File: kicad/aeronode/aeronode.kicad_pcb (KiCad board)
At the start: 4 copper layers, 90 x 70 mm, 77 parts, among them J1 IMU_BOARD, J2 USB-C PD / recovery, J3 2S LiFePO4 6Ah + BMS, Q1 NMOS pass - TBD, SW1 ON/OFF, U1 ConnectCore93_LGA, U10 BMP390, U2 CYPD3177-24LQ, U3 BQ25798, U4 LMR33630ADDA, U5 LTC4364CMS, U6 BME690, U7 DAN-F10N, U9 MMC5983MA

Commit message: [LIMA] kicad: FIX - USB-C ground was never connected to system GND
J2's four GND pins (A1/A12/B1/B12) are stacked on one connection point in the
USB_C_Receptacle_USB2.0_16P symbol, so they formed their own 4-node net
'Net-(J2-GND-PadA1)' with no wire and no label attaching them to /GND. The
SHIELD pin was likewise floating. /GND had 254 nodes and J2 was not among them.

Impact if built: VBUS arrives with no return path. No charging, no PD
negotiation, CC1/CC2 with no ground reference - the board is dead on USB.

ERC did not surface it usefully: the pins are connected to EACH OTHER, so they
are not 'unconnected pins', and the design already carries 170 pin_not_connected
warnings from unused CC93 pads, which buries anything real. It was found by
inspecting net pad-counts while planning the ground plane.

Fix: added GND labels at (149.86,642.62) and (142.24,642.62) - this schematic
uses local labels, not power symbols, so that is the idiomatic form here.
/GND now 259 nodes with J2 A1/A12/B1/B12/SH present, no isolated J2 nets.
Board re-bound from the corrected netlist: 8 pads changed, 0 mismatches,
DRC 0 violations, schematic parity 0.

Shield is tied directly to GND. Standard for a board with no separate chassis
ground, but revisit if the enclosure needs a decoupled shield connection.

Co-Authored-By: Claude Opus 5 <noreply@anthropic.com>
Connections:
- J2 pad A1: Net-(J2-GND-PadA1) -> /GND
- J2 pad A12: Net-(J2-GND-PadA1) -> /GND
- J2 pad B1: Net-(J2-GND-PadA1) -> /GND
- J2 pad B12: Net-(J2-GND-PadA1) -> /GND
- J2 pad SH: unconnected-(J2-SHIELD-PadSH) -> /GND
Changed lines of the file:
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@@
 			(layers "F.Cu" "F.Mask" "F.Paste")
 			(roundrect_rratio 0.25)
-			(net "Net-(J2-GND-PadA1)")
+			(net "/GND")
 		)
 		(pad "A4" smd roundrect
@@
 			(layers "F.Cu" "F.Mask" "F.Paste")
 			(roundrect_rratio 0.25)
-			(net "Net-(J2-GND-PadA1)")
+			(net "/GND")
 		)
 		(pad "B1" smd roundrect
@@
 			(layers "F.Cu" "F.Mask" "F.Paste")
 			(roundrect_rratio 0.25)
-			(net "Net-(J2-GND-PadA1)")
+			(net "/GND")
 		)
 		(pad "B4" smd roundrect
@@
 			(layers "F.Cu" "F.Mask" "F.Paste")
 			(roundrect_rratio 0.25)
-			(net "Net-(J2-GND-PadA1)")
+			(net "/GND")
 		)
 		(pad "SH" thru_hole oval
@@
 			(layers "*.Cu" "*.Mask")
 			(remove_unused_layers no)
-			(net "unconnected-(J2-SHIELD-PadSH)")
+			(net "/GND")
 		)
 		(pad "SH" thru_hole oval
@@
 			(layers "*.Cu" "*.Mask")
 			(remove_unused_layers no)
-			(net "unconnected-(J2-SHIELD-PadSH)")
+			(net "/GND")
 		)
 		(pad "SH" thru_hole oval
@@
 			(layers "*.Cu" "*.Mask")
 			(remove_unused_layers no)
-			(net "unconnected-(J2-SHIELD-PadSH)")
+			(net "/GND")
 		)
 		(pad "SH" thru_hole oval
@@
 			(layers "*.Cu" "*.Mask")
 			(remove_unused_layers no)
-			(net "unconnected-(J2-SHIELD-PadSH)")
+			(net "/GND")
 		)
 		(embedded_fonts no)

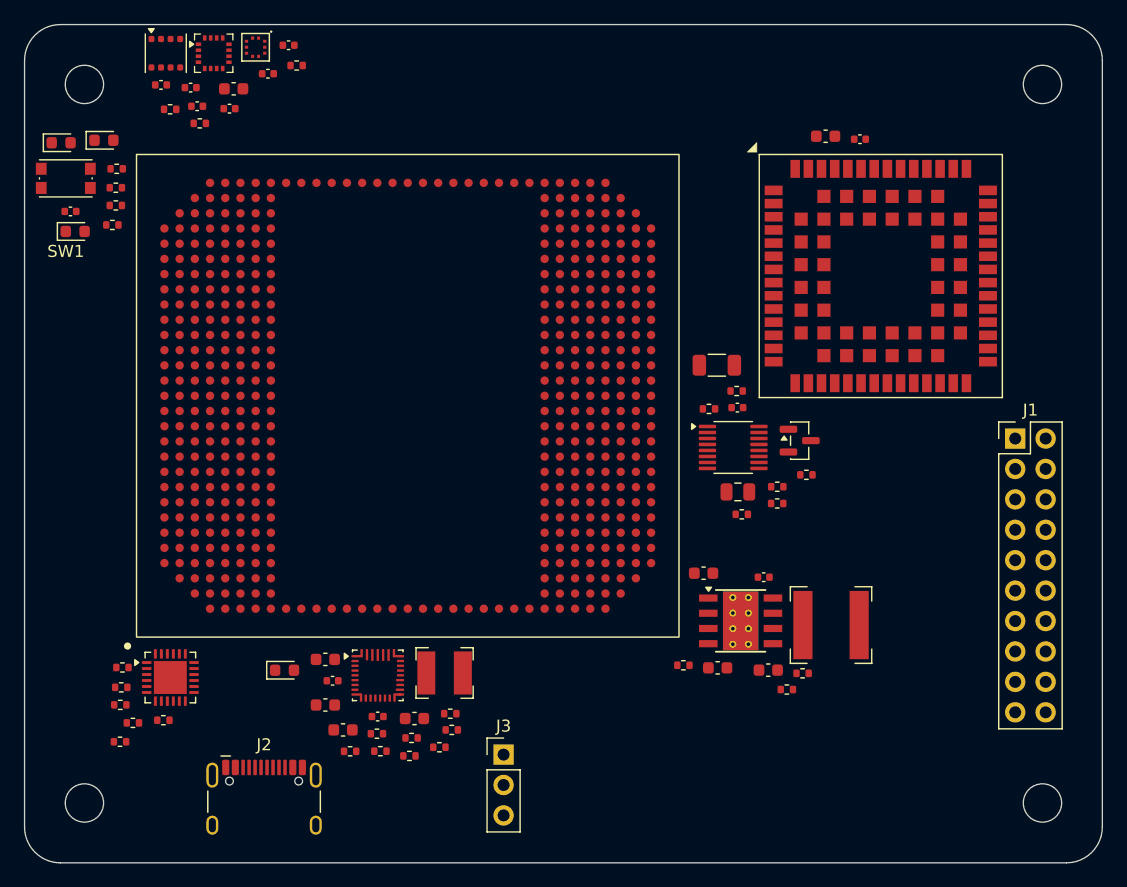
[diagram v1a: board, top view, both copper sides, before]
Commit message: [LIMA] kicad: add GND/+3V3 planes, net classes and via stitching
Stackup now SIG/GND/PWR/SIG: solid GND plane on In1 under F.Cu so top-layer
signals reference an unbroken return; +3V3 plane on In2 (the only rail spanning
the whole board, 37 pads across x 26.8..102.7). Localised rails stay as traces.

Net classes: Default 0.20mm, Power 0.50mm, HighCurrent 1.00mm. All at 0.20mm
clearance - HighCurrent started at 0.25mm and failed against fixed IC pin pitch
inside U3/U5; current is carried by width, not clearance.

266 GND stitching vias on a 4mm grid tie the pours to the In1 plane. 31 of 37
+3V3 pads have a fanout via to In2; 6 failed in the tight sensor cluster and
need hand routing or a smaller local via.

DRC 0 violations, parity 0, unconnected 468 -> 141.

Four bugs in my own via placement, all caught by DRC and all recorded:
- 0.25mm drills below the 0.30mm board minimum
- hole-to-hole check skipped same-net pads, but hole spacing is net-independent;
  GND vias landed 0.08mm from J1's GND through-holes
- track PATHS were never validated, only via positions, so tracks crossed pads
  and shorted +3V3 to BAT_TS and to U10's INT pin
- dangling vias where the pour did not reach
Lesson: validating an endpoint is not validating a connection.

Also recorded a KiCad SWIG trap: board.Remove() in a loop leaves GetTracks()/
GetFootprints() returning raw SwigPyObjects. Save and reload between bulk
deletion and rebuild.

Signal routing is NOT done - no autorouter is available.

Co-Authored-By: Claude Opus 5 <noreply@anthropic.com>
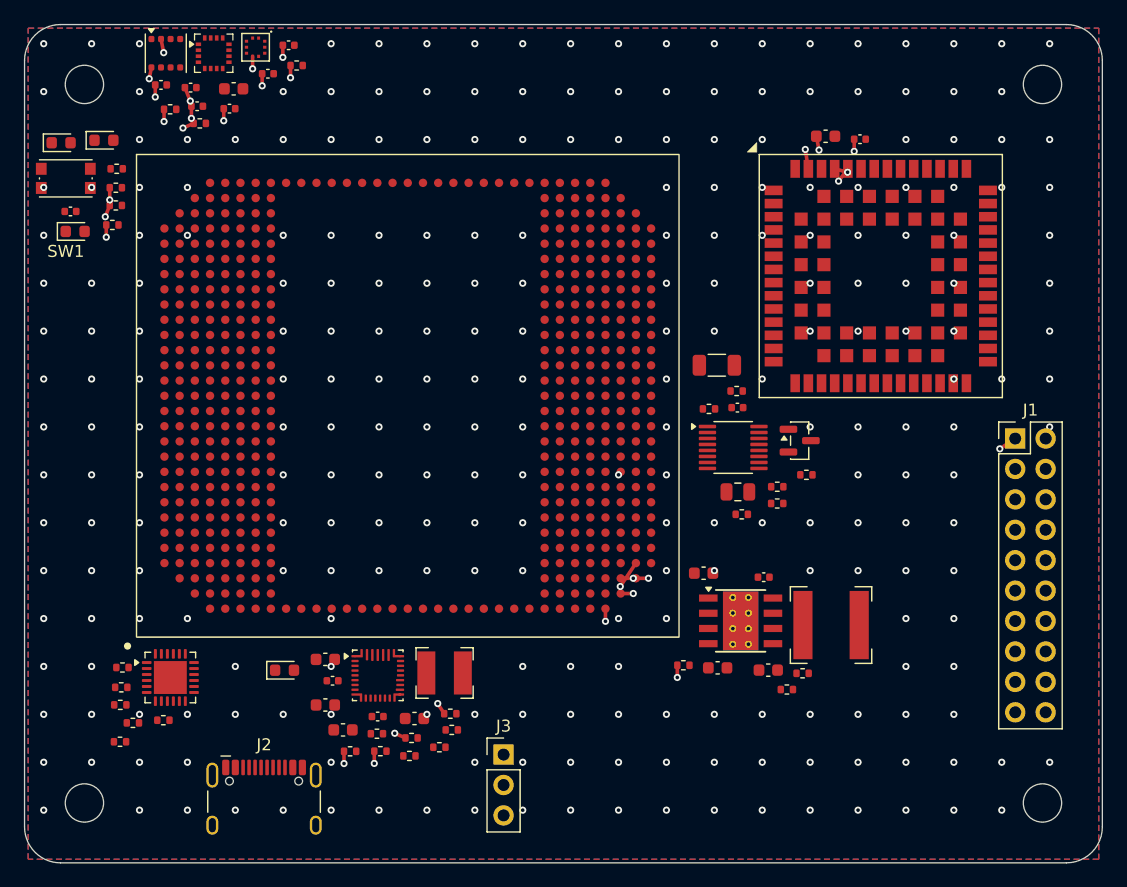
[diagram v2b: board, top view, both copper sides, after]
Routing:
- net /+3V3: track 0.00 -> 34.9 mm, vias 0 -> 31
- net /GND: vias 0 -> 266
- added copper zone on In2.Cu, net /+3V3
- added copper zone on B.Cu, net /GND
- added copper zone on F.Cu, net /GND
- added copper zone on In1.Cu, net /GND

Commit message: [LIMA] kicad: autoroute with Freerouting - 525 tracks, DRC 0, unconnected 468->59
Installed Freerouting v2.3.0 (official GitHub release, SHA-256 3cf18d60...0ee24)
plus OpenJDK 25 - v2.3.0 needs class file version 69, Java 21 is rejected.
kicad-cli has no Specctra DSN export; pcbnew's Python ExportSpecctraDSN /
ImportSpecctraSES provide the round-trip headlessly.

Three runs; only the third had a valid input:

1. Seeding the DSN with my own 297 stitching vias + 31 tracks was actively
   harmful. The DSN exports them as (type route) - rippable, not fixed - so
   they protected nothing and were 96 of the 116 violations the router had to
   work around every pass. Violations frozen from pass 1; passes hit 28 min.
   Stitching vias belong AFTER routing.

2. The 'clean' run completed but was unusable: net classes live in the
   .kicad_pro, not the .kicad_pcb. Copying only the board to a scratch dir
   lost them, so everything routed at 0.2mm - including VBUS, +5V_RAW and
   VSYS_CHG which need 1.0mm for the 3A charger path.

3. Clean input + all 3 classes: 41 unrouted / 70 router violations, cleaned
   to DRC 0. Width histogram confirms classes applied: 36 tracks at 1.0mm,
   125 at 0.5mm.

Retracting my own claim: I asserted the bottleneck was committing both inner
layers to planes. Measured - 3 signal layers gave 49.2% fanout vs 49.9% for 2.
The layer count was never the constraint. Asserting before measuring cost ~90
minutes of compute.

Cleanup 36->13->4->1->0: widened 32 sub-minimum tracks, removed dangling vias
and orphaned stubs, refilled between each. Removing a dangling item can orphan
its neighbour, so cleanup must iterate to a fixed point.

Then 214 GND stitching vias placed post-routing avoiding pads, tracks and the
router's vias; 45 unreachable ones removed by the same loop; 169 live.

Remaining: 59 unconnected over 34 nets, concentrated in the charger corner
where 1.0mm HighCurrent tracks compete for space. Needs hand routing.

Co-Authored-By: Claude Opus 5 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
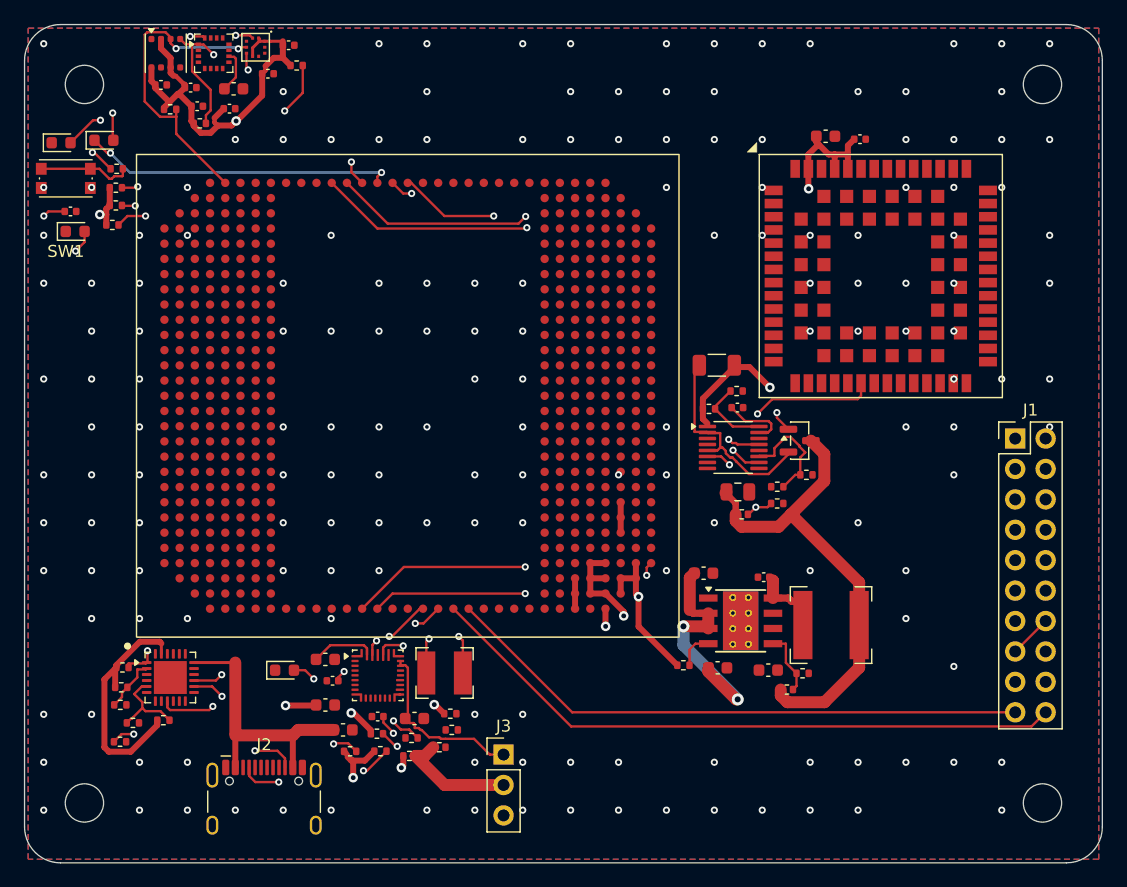
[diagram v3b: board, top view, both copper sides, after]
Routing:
- net /BMI_MOSI: track 0.00 -> 72.4 mm, vias 0 -> 1
- net /BMI_SCLK: track 0.00 -> 70.4 mm, vias 0 -> 1
- net /BMI_ACC_CS: track 0.00 -> 61.4 mm, vias 0 -> 1
- net /BMI_SDO: track 0.00 -> 59.4 mm, vias 0 -> 1
- net /PD_FAULT: track 0.00 -> 56.9 mm, vias 0 -> 2
- net /BMI_GYR_INT: track 0.00 -> 54.0 mm
- net /BMI_ACC_INT: track 0.00 -> 49.2 mm
- net /+5V: track 0.00 -> 48.5 mm, vias 0 -> 2
- net /GNSS_PPS: track 0.00 -> 47.5 mm, vias 0 -> 2
- net /OVP_FLT_N: track 0.00 -> 39.6 mm, vias 0 -> 2
- net /+5V_RAW: track 0.00 -> 39.5 mm
- net /CHG_CE_N: track 0.00 -> 34.2 mm, vias 0 -> 2
- net /+3V3: track 34.9 -> 68.8 mm, vias 31 -> 7
- net /I2C4_SDA: track 0.00 -> 29.0 mm, vias 0 -> 3
- net /LED_BLU_N: track 0.00 -> 26.1 mm, vias 0 -> 2
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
